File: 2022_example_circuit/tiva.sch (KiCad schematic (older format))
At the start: 1 part, among them U3 TM4C129E_Launchpad

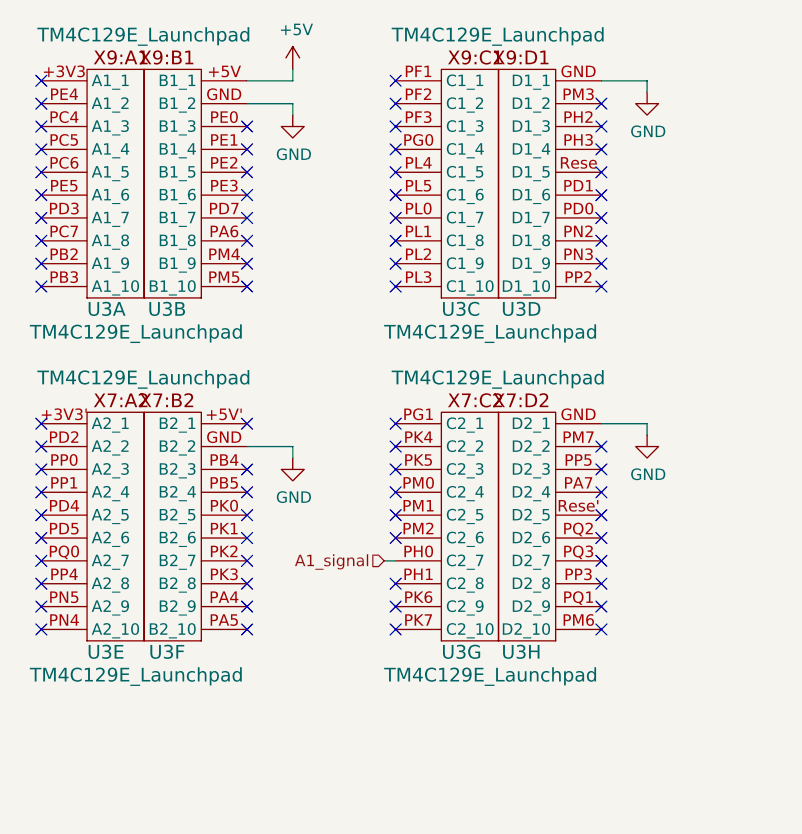
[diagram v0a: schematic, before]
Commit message: Created Schematic for Training Hardware
Schematic for:
LT1910 MOSFET Driver
Andersons
5V Buck Converter
3V3 Buck Converter
Tiva (hierarchical sheet)
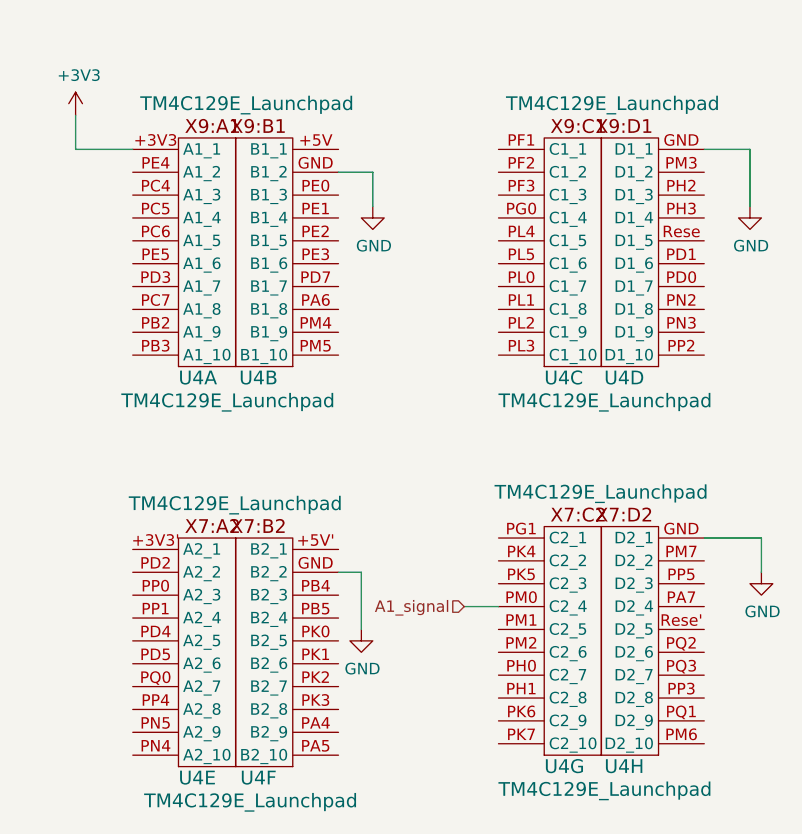
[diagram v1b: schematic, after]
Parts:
- removed U3: TM4C129E_Launchpad, MRDT_Shields:TM4C129E_Launchpad_FULL_THT_TOP, symbol MRDT_Shields:TM4C129E_Launchpad
- added U4: TM4C129E_Launchpad, symbol MRDT_Shields:TM4C129E_Launchpad
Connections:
- net A1_signal: now also U4.PM0 (C2_4)
- net GND: now also U4.GND (B1_2), U4.GND (B2_2), U4.GND (D1_1), U4.GND (D2_1)
- new net +3V3: U4.+3V3 (A1_1)
- no-connect marks 74 -> 0
